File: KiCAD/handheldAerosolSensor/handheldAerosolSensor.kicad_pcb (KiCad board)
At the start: 2 copper layers, 99.8 x 86.4 mm, 16 parts, among them J3 I2C 3v3, J4 SPS30, Q1 AO3401, Q2 BSS138, SW1 PWR, U1 ESP32-DEVKIT-V1 30pin, U2 Mini DC-DC Convertor

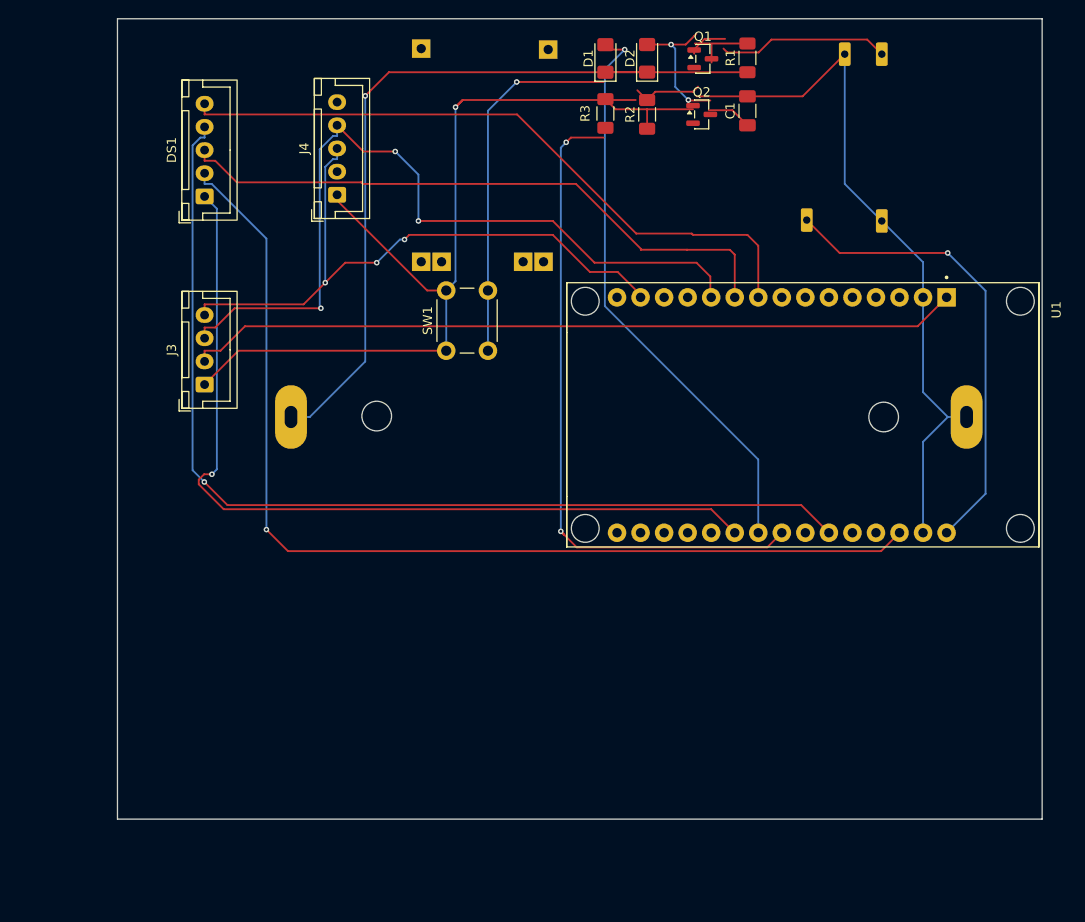
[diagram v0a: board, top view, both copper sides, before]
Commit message: feat(hardware): Add buzzer and reorganize PCB net naming
- Add CPI-148-24-90T-67 buzzer/transducer component (LS1)
- Refactor battery net names for consistency (BAT → BATT, BATT-SW)
- Reorganize net numbering and clean up net naming scheme
- Update component references and power connections
- Add new footprint library entry for buzzer transducer
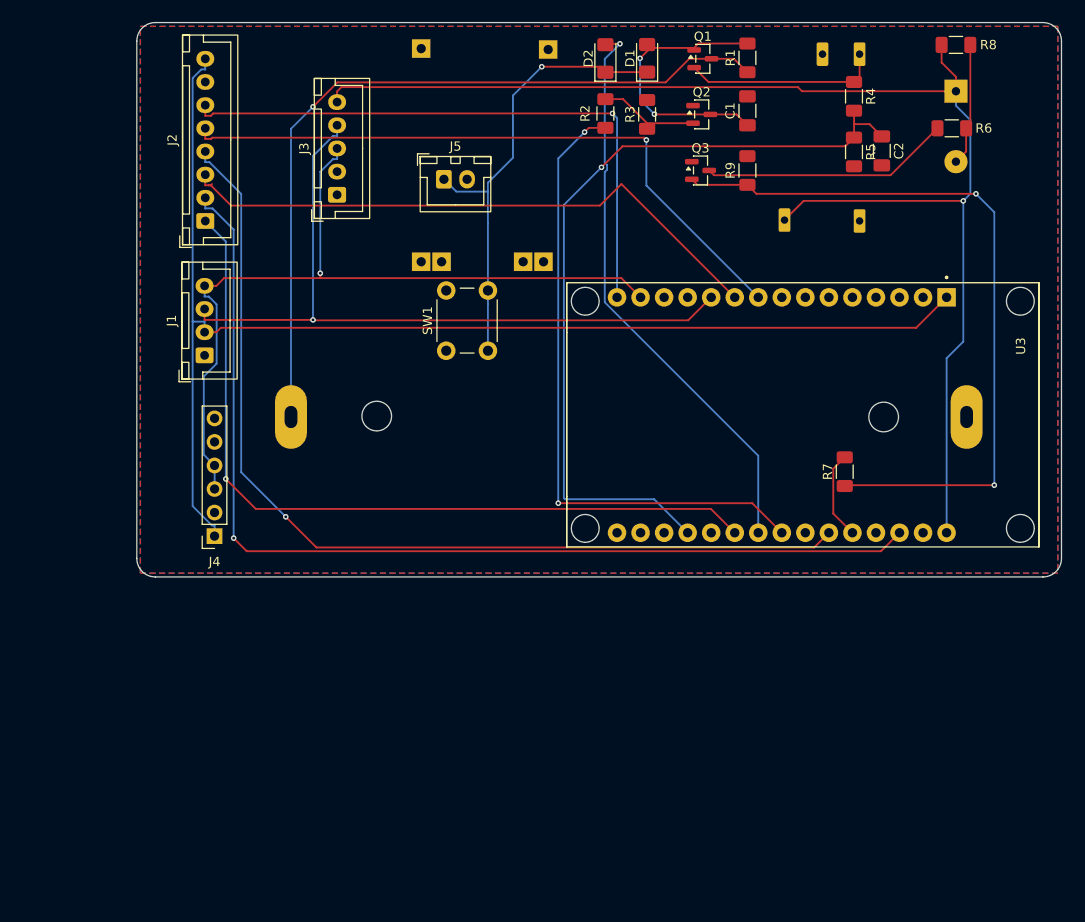
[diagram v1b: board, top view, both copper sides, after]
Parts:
- removed DS1: EPAPER_SPI_DISPLAY, Connector_JST:JST_XH_B5B-XH-A_1x05_P2.50mm_Vertical
- added C2: 0.1uF, Capacitor_SMD:C_1206_3216Metric_Pad1.33x1.80mm_HandSolder, F.Cu at (207.5, 57.4)
- added J2: ePaper, Connector_JST:JST_XH_B8B-XH-A_1x08_P2.50mm_Vertical, F.Cu at (134.5, 65.0)
- added J4: MBE/P280, Connector_PinSocket_2.54mm:PinSocket_1x06_P2.54mm_Vertical, F.Cu at (135.5, 99.0)
- added J5: Ext.Sw, Connector_JST:JST_XH_B2B-XH-A_1x02_P2.50mm_Vertical, F.Cu at (160.2, 60.5)
- added LS1: PIEZO, MyNewLibrary:XDCR_CPI-148-24-90T-67, B.Cu at (215.5, 54.8)
- added Q3: BSS138, Package_TO_SOT_SMD:SOT-23, F.Cu at (187.9, 59.5)
- added R4: 100k, Resistor_SMD:R_1206_3216Metric_Pad1.30x1.75mm_HandSolder, F.Cu at (204.5, 51.5)
- added R5: 100k, Resistor_SMD:R_1206_3216Metric_Pad1.30x1.75mm_HandSolder, F.Cu at (204.5, 57.5)
- added R6: 10R-220R, Resistor_SMD:R_1206_3216Metric_Pad1.30x1.75mm_HandSolder, F.Cu at (215.1, 55.0)
- added R7: 1k, Resistor_SMD:R_1206_3216Metric_Pad1.30x1.75mm_HandSolder, F.Cu at (203.5, 92.0)
- added R8: 2k2, Resistor_SMD:R_1206_3216Metric_Pad1.30x1.75mm_HandSolder, F.Cu at (215.5, 46.0)
- added R9: 100k, Resistor_SMD:R_1206_3216Metric_Pad1.30x1.75mm_HandSolder, F.Cu at (193.0, 59.5)
- moved J1 3.15 mm to (134.4, 79.5)
- moved U2 2.40 mm to (201.0, 56.1)
- renumbered D2 to D1, D1 to D2, J3 to J1, J4 to J3, R3 to R2, R2 to R3, U3 to U1, U1 to U3
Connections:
- net +BATT renamed BATT
- net Net-(Q1-D) renamed BATT-SW
- J3 pad 2: SEL -> GND
- J3 pad 5: 5v -> +5v
- U3 pad 19: BAT -> Net-(U3-D34)
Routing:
- net GND: track 177.5 -> 0.00 mm, vias 1 -> 0
- net +5v: track 50.3 -> 143.4 mm
- net Net-(U3-D34): track 0.00 -> 87.3 mm, vias 0 -> 1
- net Net-(Q3-G): track 0.00 -> 79.7 mm, vias 0 -> 2
- net EPD_MOSI(DIN): track 0.00 -> 65.2 mm, vias 0 -> 1
- net 3v3: track 83.6 -> 137.5 mm
- net Net-(Q3-D): track 0.00 -> 26.9 mm
- net SCL: track 69.5 -> 87.0 mm, vias 3 -> 1
- net Net-(LS1-PadN): track 0.00 -> 13.2 mm
- net BUZZER: track 0.00 -> 9.51 mm
- net SDA: track 87.6 -> 79.2 mm, vias 3 -> 1
- net EPD_BUSY: track 92.9 -> 86.1 mm
- net Net-(D1-K): track 44.2 -> 50.0 mm
- net EPD_CS: track 109.3 -> 103.9 mm
- net LATCH: track 72.8 -> 69.1 mm
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- added copper zone on B.Cu, net GND
- added copper zone on F.Cu, net GND
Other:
- board size 99.8 x 86.4 mm -> 99.8 x 59.8 mm

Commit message: KiCad aanpassingen
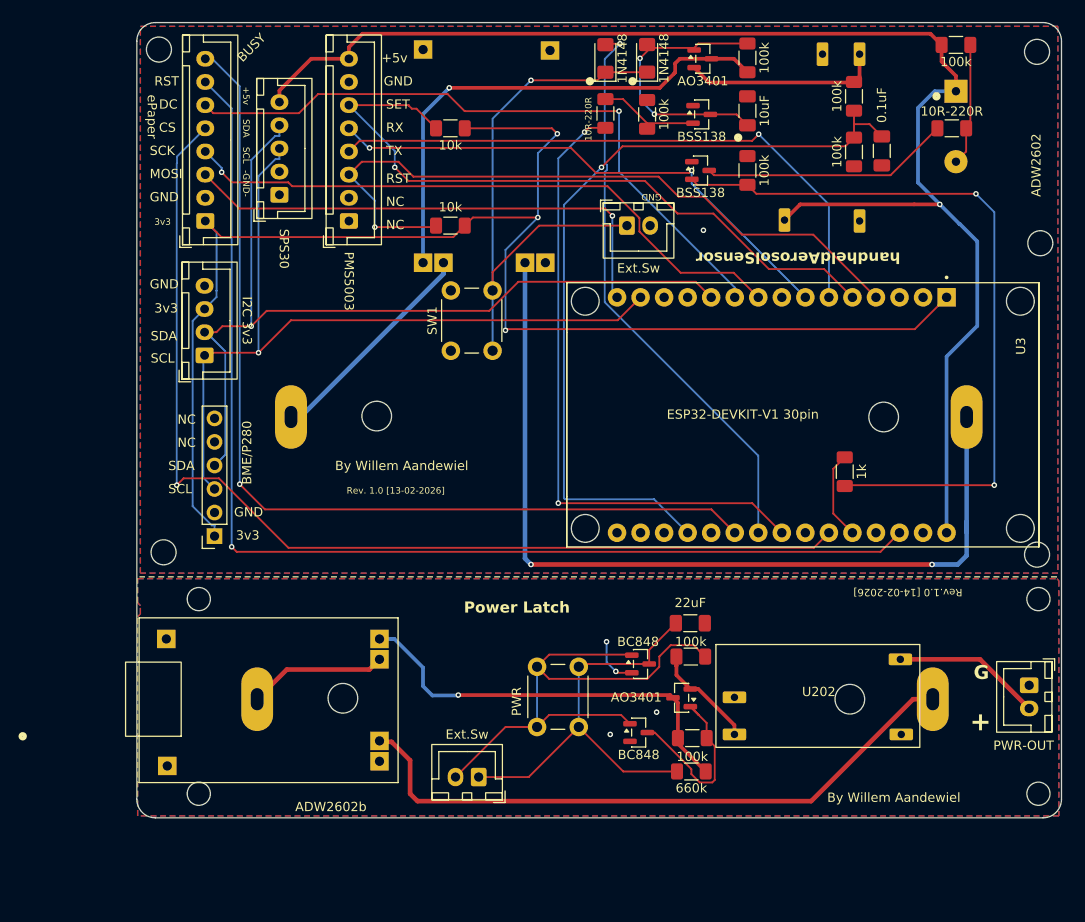
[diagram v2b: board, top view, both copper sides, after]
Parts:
- added BT201: BH-18650-PC, MyNewLibrary:BAT_BH-18650-PC, B.Cu at (176.6, 116.6)
- added C201: 22uF, Capacitor_SMD:C_1206_3216Metric_Pad1.33x1.80mm_HandSolder, F.Cu at (186.8, 108.4)
- added H1: MountingHole, MountingHole:MountingHole_2.7mm, F.Cu at (129.5, 46.5)
- added H2: MountingHole, MountingHole:MountingHole_2.7mm, F.Cu at (224.2, 46.8)
- added H201: MountingHole, MountingHole:MountingHole_2.5mm, F.Cu at (133.8, 105.8)
- added H202: MountingHole, MountingHole:MountingHole_2.5mm, F.Cu at (224.4, 105.8)
- added H203: MountingHole, MountingHole:MountingHole_2.5mm, F.Cu at (224.4, 126.8)
- added H204: MountingHole, MountingHole:MountingHole_2.5mm, F.Cu at (133.8, 126.8)
- added H3: MountingHole, MountingHole:MountingHole_2.7mm, F.Cu at (224.2, 101.0)
- added H4: MountingHole, MountingHole:MountingHole_2.7mm, F.Cu at (130.0, 100.8)
- added H5: MountingHole, MountingHole:MountingHole_2.7mm, F.Cu at (224.6, 67.4)
- added J201: PWR-OUT, Connector_JST:JST_XH_B2B-XH-A_1x02_P2.50mm_Vertical, F.Cu at (223.4, 115.1)
- added J202: Ext.Sw, Connector_JST:JST_XH_B2B-XH-A_1x02_P2.50mm_Vertical, F.Cu at (164.0, 125.0)
- added J6: PMS5003, Connector_JST:JST_XH_B8B-XH-A_1x08_P2.50mm_Vertical, F.Cu at (150.0, 65.0)
- added Q201: AO3401, Package_TO_SOT_SMD:SOT-23, F.Cu at (185.9, 116.5)
- added Q202: BC848, Package_TO_SOT_SMD:SOT-23, F.Cu at (181.3, 120.2)
- added Q203: BC848, Package_TO_SOT_SMD:SOT-23, F.Cu at (181.5, 112.8)
- added R10: 10k, Resistor_SMD:R_1206_3216Metric_Pad1.30x1.75mm_HandSolder, F.Cu at (160.9, 55.0)
- added R11: 10k, Resistor_SMD:R_1206_3216Metric_Pad1.30x1.75mm_HandSolder, F.Cu at (160.9, 65.5)
- added R201: 100k, Resistor_SMD:R_1206_3216Metric_Pad1.30x1.75mm_HandSolder, F.Cu at (187.1, 120.8)
- added R202: 100k, Resistor_SMD:R_1206_3216Metric_Pad1.30x1.75mm_HandSolder, F.Cu at (186.9, 112.0)
- added R203: 660k, Resistor_SMD:R_1206_3216Metric_Pad1.30x1.75mm_HandSolder, F.Cu at (186.9, 124.4)
- added SW201: PWR, Button_Switch_THT:SW_PUSH_6mm_H4.3mm, F.Cu at (174.8, 113.1)
- added U201: ~, MyNewLibrary:TP4056_USB-Charger_Board, F.Cu at (140.9, 116.6)
- added U202: Mini DC-DC Convertor, MyNewLibrary:Mini DC-DC Boost Convertor, F.Cu at (200.7, 116.3)
- D1, D2: value D_Filled -> 1N4148
- J4: value MBE/P280 -> BME/P280
- R8: value 2k2 -> 100k
- moved J5 20.4 mm to (180.0, 65.5)
- moved J3 6.22 mm to (142.5, 62.2)
- moved SW1 0.50 mm to (161.0, 79.0)
- moved U1 0.22 mm to (164.5, 57.1)
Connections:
- BT1 pad N: GND -> B-
- BT1 pad P: BATT -> B+
- J1 pad 1: GND -> SCL
- J1 pad 2: 3v3 -> SDA
- J1 pad 3: SDA -> 3v3
- J1 pad 4: SCL -> GND
- J2 pad 1: EPD_BUSY -> 3v3
- J2 pad 2: EPD_RST -> GND
- J2 pad 3: EPD_DC -> EPD_MOSI(DIN)
- J2 pad 4: EPD_CS -> EPS_SCK
- J2 pad 5: EPS_SCK -> EPD_CS
- J2 pad 6: EPD_MOSI(DIN) -> EPD_DC
- J2 pad 7: GND -> EPD_RST
- J2 pad 8: 3v3 -> EPD_BUSY
- J4 pad 4: SCL -> SDA
- Q1 pad 3: BATT -> OUT+
- R1 pad 1: BATT -> OUT+
- U3 pad 4: unconnected-(U3-D2-Pad4) -> PMS5003-RESET
- U3 pad 5: unconnected-(U3-D4-Pad5) -> PMS5003-SET
- U3 pad 6: RX2 -> RX2-PMS5003-TX
- U3 pad 7: TX2 -> TX2-PMS5003-RX
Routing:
- net B-: track 0.00 -> 96.2 mm, vias 0 -> 2
- net BATT: track 84.1 -> 0.00 mm, vias 1 -> 0
- net PMS5003-RESET: track 0.00 -> 77.0 mm, vias 0 -> 1
- net PMS5003-SET: track 0.00 -> 74.4 mm, vias 0 -> 1
- net B2BAT-: track 0.00 -> 69.1 mm
- net RX2-PMS5003-TX: track 0.00 -> 65.7 mm, vias 0 -> 1
- net Net-(J202-Pin_2): track 0.00 -> 61.5 mm
- net TX2-PMS5003-RX: track 0.00 -> 57.9 mm, vias 0 -> 2
- net OUT+: track 0.00 -> 54.7 mm, vias 0 -> 1
- net Net-(J202-Pin_1): track 0.00 -> 45.4 mm
- net OUT2+: track 0.00 -> 45.0 mm, vias 0 -> 1
- net B+: track 0.00 -> 24.1 mm
- net Net-(Q201-G): track 0.00 -> 20.2 mm
- net 3v3: track 137.5 -> 157.0 mm, vias 0 -> 3
- net SDA: track 79.2 -> 96.7 mm
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- added copper zone on B.Cu, net GND2
- added copper zone on F.Cu, net GND2
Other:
- board size 99.8 x 59.8 mm -> 99.8 x 85.8 mm
- board text added: "+"
- board text added: "+5v"
- board text added: "-"
- board text added: "-GND-"
- board text added: "3v3"
- board text added: "ADW2602"
- board text added: "ADW2602b"
- board text added: "BUSY"
- board text added: "By Willem Aandewiel"
- board text added: "CS"
- board text added: "DC"
- board text added: "G"
- board text added: "GND"
- board text added: "MOSI"
- board text added: "NC"
- board text added: "Power Latch"
- board text added: "RST"
- board text added: "RX"
- board text added: "Rev. 1.0 [13-02-2026]"
- board text added: "Rev.1.0 [14-02-2026]"
- board text added: "SCK"
- board text added: "SCL"
- board text added: "SDA"
- board text added: "SET"
- board text added: "TX"
- board text added: "handheldAerosolSensor"

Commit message: Add power indicator LED (D201) with supporting components to the PCB design: - Add 1206 SMD power LED with current limiting resistor - Add new nets for LED connections (Net-(C201-Pad1), Net-(D201-A)) - Update PCB plot parameters (layer selection and drill shape settings) - Adjust component placement for R6 resistor - Update design date to 2026-02-15
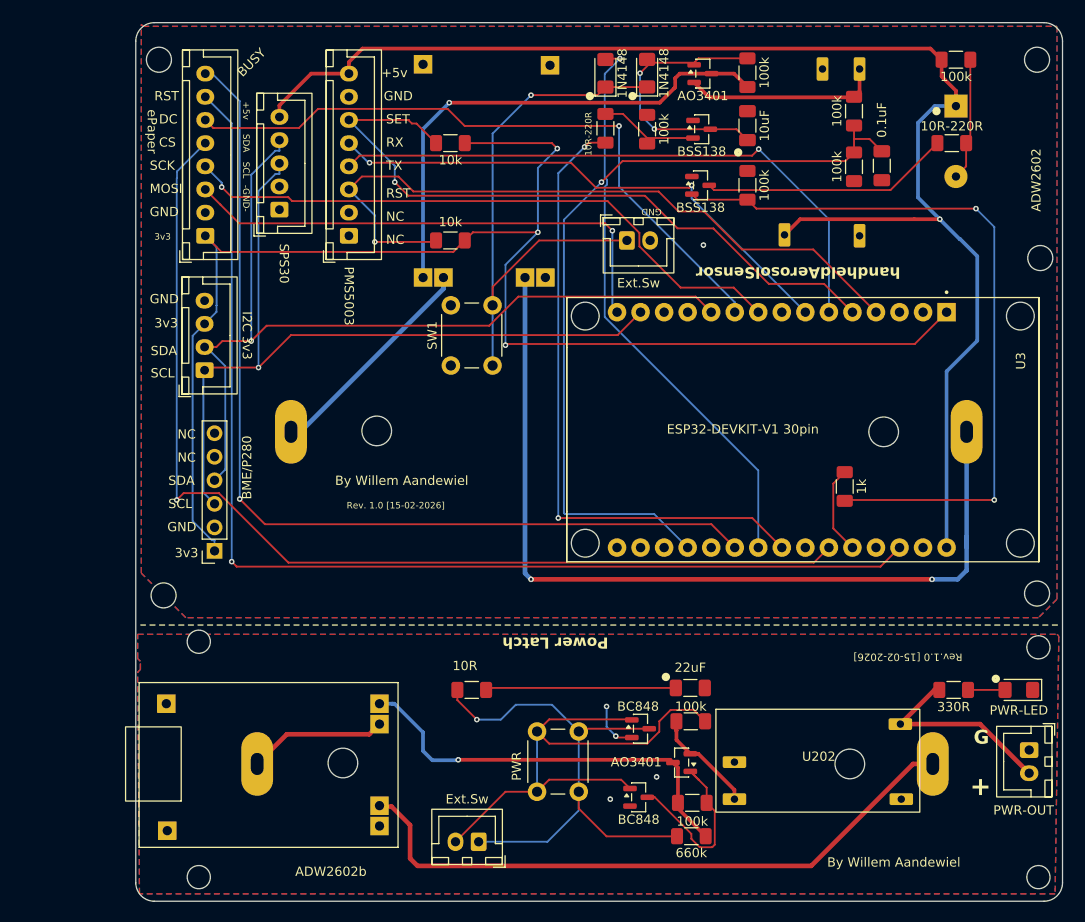
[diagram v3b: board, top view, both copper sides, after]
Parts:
- added D201: PWR-LED, LED_SMD:LED_1206_3216Metric_Pad1.42x1.75mm_HandSolder, F.Cu at (222.3, 115.6)
- added R204: 330R, Resistor_SMD:R_1206_3216Metric_Pad1.30x1.75mm_HandSolder, F.Cu at (215.2, 115.6)
- added R205: 10R, Resistor_SMD:R_1206_3216Metric_Pad1.30x1.75mm_HandSolder, F.Cu at (163.2, 115.6)
- moved H203 9.00 mm to (224.4, 135.8)
- moved H204 9.00 mm to (133.8, 135.8)
- moved BT201 6.99 mm to (176.6, 123.6)
- moved J201 6.99 mm to (223.4, 122.1)
- moved Q203 6.99 mm to (181.5, 119.8)
- moved R201 6.99 mm to (187.1, 127.8)
- moved R202 6.99 mm to (186.9, 119.0)
- moved SW201 6.99 mm to (174.8, 120.1)
- moved U201 6.99 mm to (140.9, 123.6)
- moved U202 6.99 mm to (200.7, 123.3)
- moved C201 6.99 mm to (186.8, 115.4)
- moved J202 6.99 mm to (164.0, 132.0)
- moved Q201 6.99 mm to (185.9, 123.4)
- moved Q202 6.99 mm to (181.3, 127.2)
- moved R203 6.99 mm to (186.9, 131.4)
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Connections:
- C201 pad 1: Net-(J202-Pin_1) -> Net-(C201-Pad1)
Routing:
- net Net-(C201-Pad1): track 0.00 -> 20.6 mm
- net Net-(J202-Pin_1): track 45.4 -> 59.0 mm, vias 0 -> 1
- net +B5v: track 16.1 -> 21.8 mm
- net Net-(D201-A): track 0.00 -> 4.00 mm
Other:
- board size 99.8 x 85.8 mm -> 100 x 94.8 mm
- board text added: "Rev. 1.0 [15-02-2026]"
- board text added: "Rev.1.0 [15-02-2026]"
- board text removed: "Rev. 1.0 [13-02-2026]"
- board text removed: "Rev.1.0 [14-02-2026]"
